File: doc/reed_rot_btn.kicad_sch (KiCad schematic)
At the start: 9 parts, among them SW1 SW_Reed_SPDT, SW2 RotaryEncoder_Switch, SW3 SW_Push

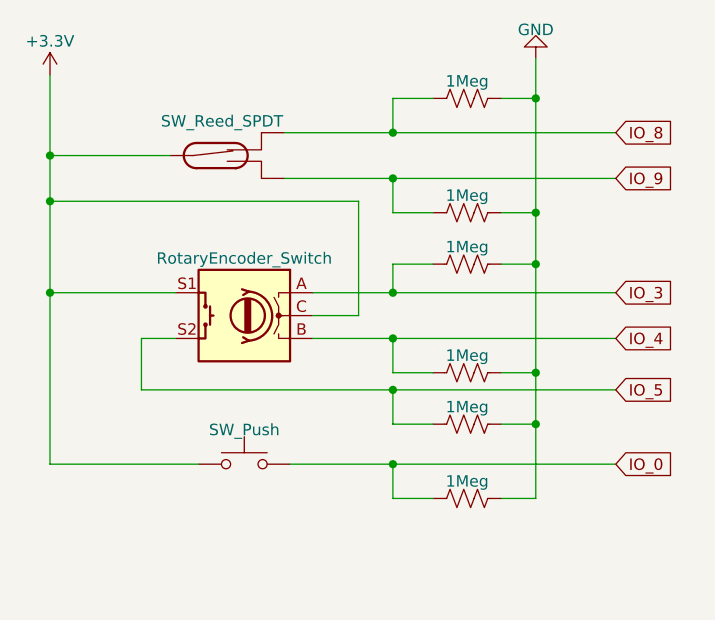
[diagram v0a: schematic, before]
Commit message: modified:   doc/Developer.md 	modified:   doc/reed_rot_btn.kicad_pro 	modified:   doc/reed_rot_btn.kicad_sch
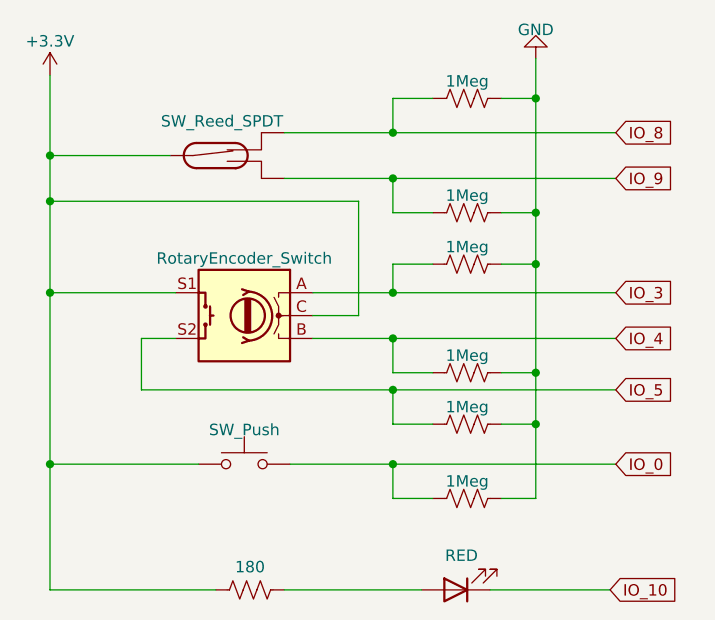
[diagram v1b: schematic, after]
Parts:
- added D101: RED, symbol Device:LED
- added R106: 180, symbol Device:R_US
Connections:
- net +3.3V: now also R106.1
- new net: D101.2 (A), R106.2
- new net IO_10: D101.1 (K)
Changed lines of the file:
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@@
   (junction (at 109.855 90.17) (diameter 0) (color 0 0 0 0)
   )
+  (junction (at 71.755 90.17) (diameter 0) (color 0 0 0 0)
+  )
   (junction (at 71.755 71.12) (diameter 0) (color 0 0 0 0)
   )
@@
     (stroke (width 0) (type default))
   )
+  (wire (pts (xy 97.79 104.14) (xy 113.03 104.14))
+    (stroke (width 0) (type default))
+  )
   (wire (pts (xy 71.755 55.88) (xy 85.09 55.88))
     (stroke (width 0) (type default))
@@
     (stroke (width 0) (type default))
   )
+  (wire (pts (xy 71.755 104.14) (xy 71.755 90.17))
+    (stroke (width 0) (type default))
+  )
   (wire (pts (xy 114.3 49.53) (xy 109.855 49.53))
     (stroke (width 0) (type default))
@@
     (stroke (width 0) (type default))
   )
+  (wire (pts (xy 120.65 104.14) (xy 133.985 104.14))
+    (stroke (width 0) (type default))
+  )
   (wire (pts (xy 114.3 62.23) (xy 109.855 62.23))
     (stroke (width 0) (type default))
@@
     (stroke (width 0) (type default))
   )
+  (wire (pts (xy 71.755 104.14) (xy 90.17 104.14))
+    (stroke (width 0) (type default))
+  )
   (wire (pts (xy 81.915 81.915) (xy 109.855 81.915))
     (stroke (width 0) (type default))
@@
     )
   )
+  (global_label "IO_10" (shape input) (at 133.985 104.14 0) (fields_autoplaced)
+    (effects (font (size 1.27 1.27)) (justify left))
+    (property "Intersheetrefs" "${INTERSHEET_REFS}" (at 142.2127 104.14 0)
+      (effects (font (size 1.27 1.27)) (justify left) hide)
+    )
+  )
   (global_label "IO_5" (shape input) (at 134.62 81.915 0) (fields_autoplaced)
     (effects (font (size 1.27 1.27)) (justify left))
@@
     )
   )
+  (symbol (lib_id "Device:LED") (at 116.84 104.14 180) (unit 1)
+    (in_bom yes) (on_board yes) (dnp no)
+    (property "Reference" "D101" (at 118.4275 97.79 0)
+      (effects (font (size 1.27 1.27)) hide)
+    )
+    (property "Value" "RED" (at 117.475 100.33 0)
+      (effects (font (size 1.27 1.27)))
+    )
+    (property "Footprint" "" (at 116.84 104.14 0)
+      (effects (font (size 1.27 1.27)) hide)
+    )
+    (property "Datasheet" "~" (at 116.84 104.14 0)
+      (effects (font (size 1.27 1.27)) hide)
+    )
+    (pin "1")
+    (pin "2")
+    (instances
+      (project "reed_rot_btn"
+        (path "/a5297d44-53ec-456a-9bfd-54aae173e634"
+          (reference "D101") (unit 1)
+        )
+      )
+    )
+  )
   (symbol (lib_id "Device:R_US") (at 118.11 93.98 90) (unit 1)
     (in_bom yes) (on_board yes) (dnp no) (fields_autoplaced)
@@
         )
       )
+    )
+  )
+  (symbol (lib_id "Device:R_US") (at 93.98 104.14 90) (unit 1)
+    (in_bom yes) (on_board yes) (dnp no) (fields_autoplaced)
+    (property "Reference" "R106" (at 93.98 99.695 90)
+      (effects (font (size 1.27 1.27)) hide)
+    )
+    (property "Value" "180" (at 93.98 101.6 90)
+      (effects (font (size 1.27 1.27)))
+    )
+    (property "Footprint" "" (at 94.234 103.124 90)
+      (effects (font (size 1.27 1.27)) hide)
+    )
+    (property "Datasheet" "~" (at 93.98 104.14 0)
+      (effects (font (size 1.27 1.27)) hide)
+    )
+    (pin "1")
+    (pin "2")
+    (instances
+      (project "reed_rot_btn"
+        (path "/a5297d44-53ec-456a-9bfd-54aae173e634"
+          (reference "R106") (unit 1)
+        )
+      )
